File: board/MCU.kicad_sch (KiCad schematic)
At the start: 2 parts, among them IC1 TLT9251VLEXUMA1, IC3 PAC55723QM-T

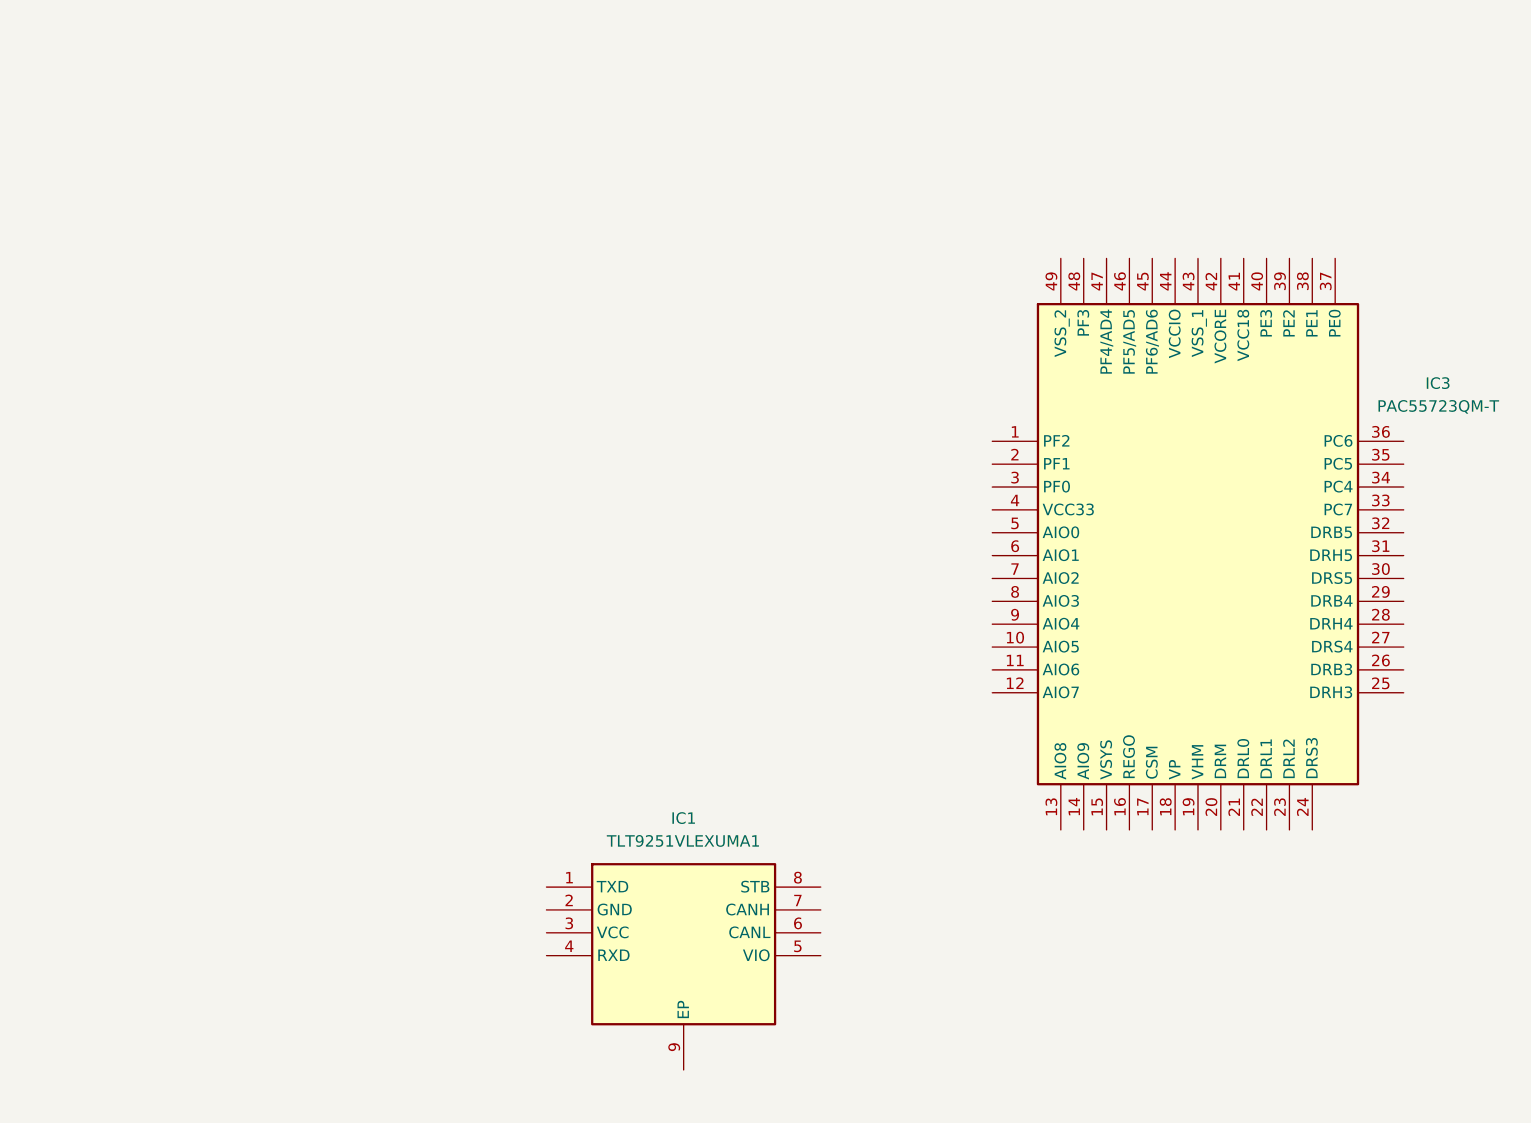
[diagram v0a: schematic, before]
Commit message: Added MCU and initial half bridge circuits from application circuit.
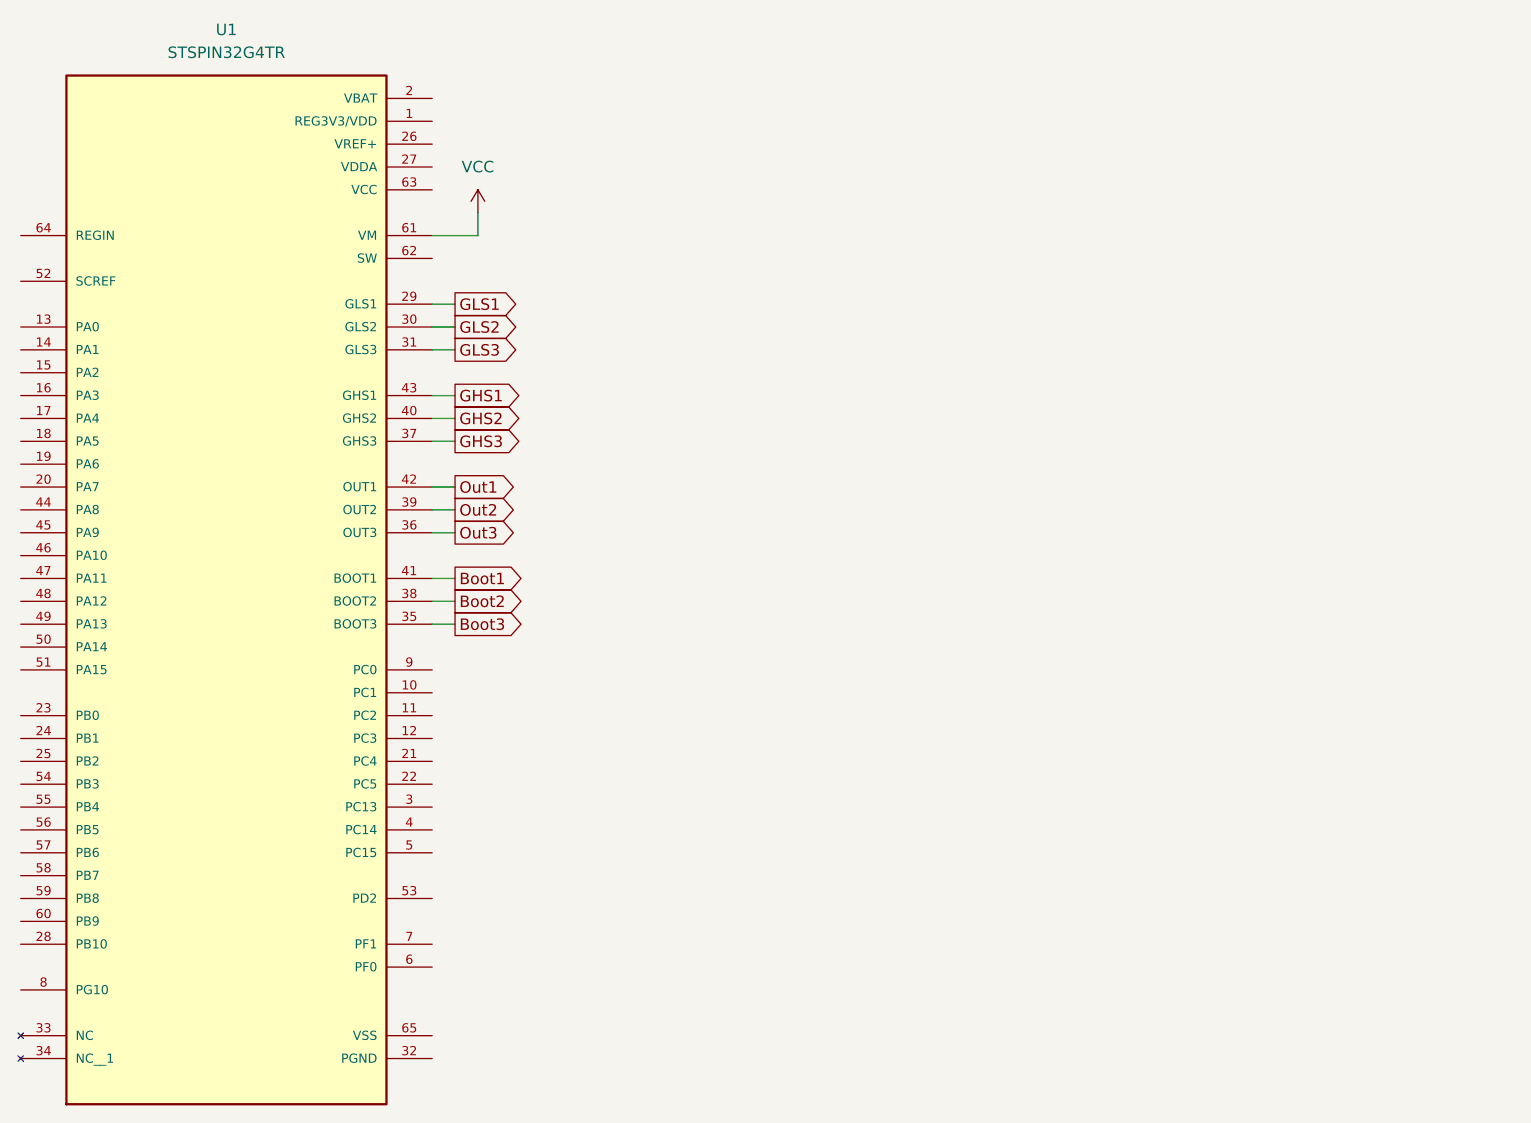
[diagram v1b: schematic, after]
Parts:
- removed IC1: TLT9251VLEXUMA1, brushless_moco_footprints:SON65P300X300X110-9N, symbol brushless_moco_symbols:TLT9251VLEXUMA1
- removed IC3: PAC55723QM-T, brushless_moco_footprints:QFN40P600X600X80-49N-D, symbol brushless_moco_symbols:PAC55723QM-T
- added U1: STSPIN32G4TR, STSPIN32G4TR:QFN50P900X900X100-65N, symbol STSPIN32G4TR:STSPIN32G4TR
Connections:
- new net Boot1: U1.41 (BOOT1)
- new net Boot2: U1.38 (BOOT2)
- new net Boot3: U1.35 (BOOT3)
- new net GHS1: U1.43 (GHS1)
- new net GHS2: U1.40 (GHS2)
- new net GHS3: U1.37 (GHS3)
- new net GLS1: U1.29 (GLS1)
- new net GLS2: U1.30 (GLS2)
- new net GLS3: U1.31 (GLS3)
- new net Out1: U1.42 (OUT1)
- new net Out2: U1.39 (OUT2)
- new net Out3: U1.36 (OUT3)
- new net VCC: U1.61 (VM)

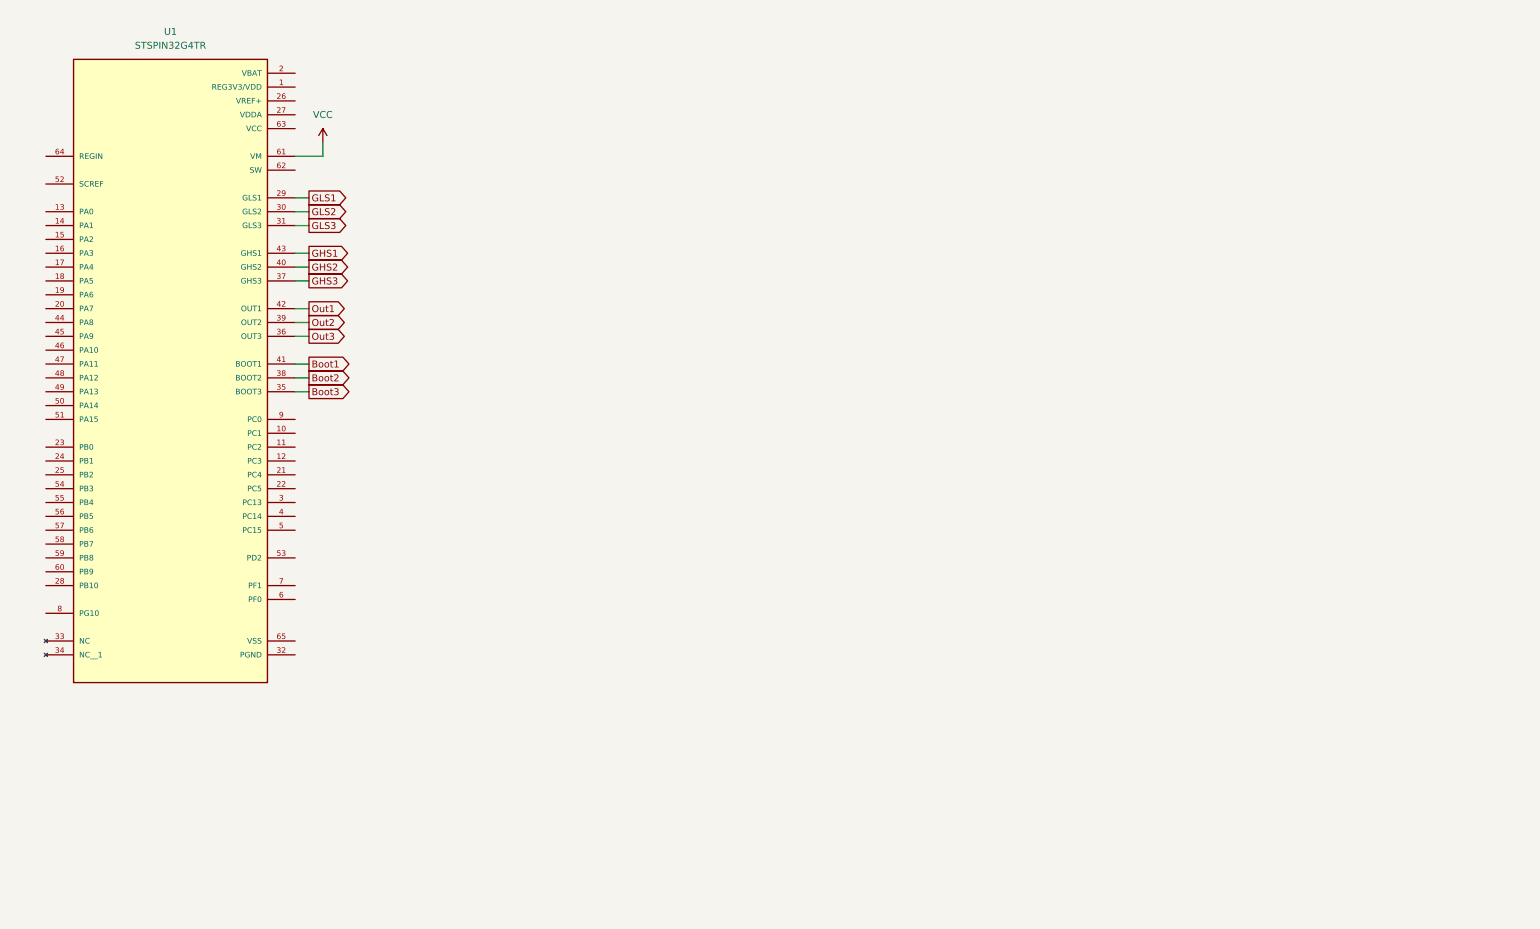
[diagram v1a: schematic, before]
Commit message: Added connections around the MCU from the application circuit from the data sheet, VCC, VDD, VREF+, etc.
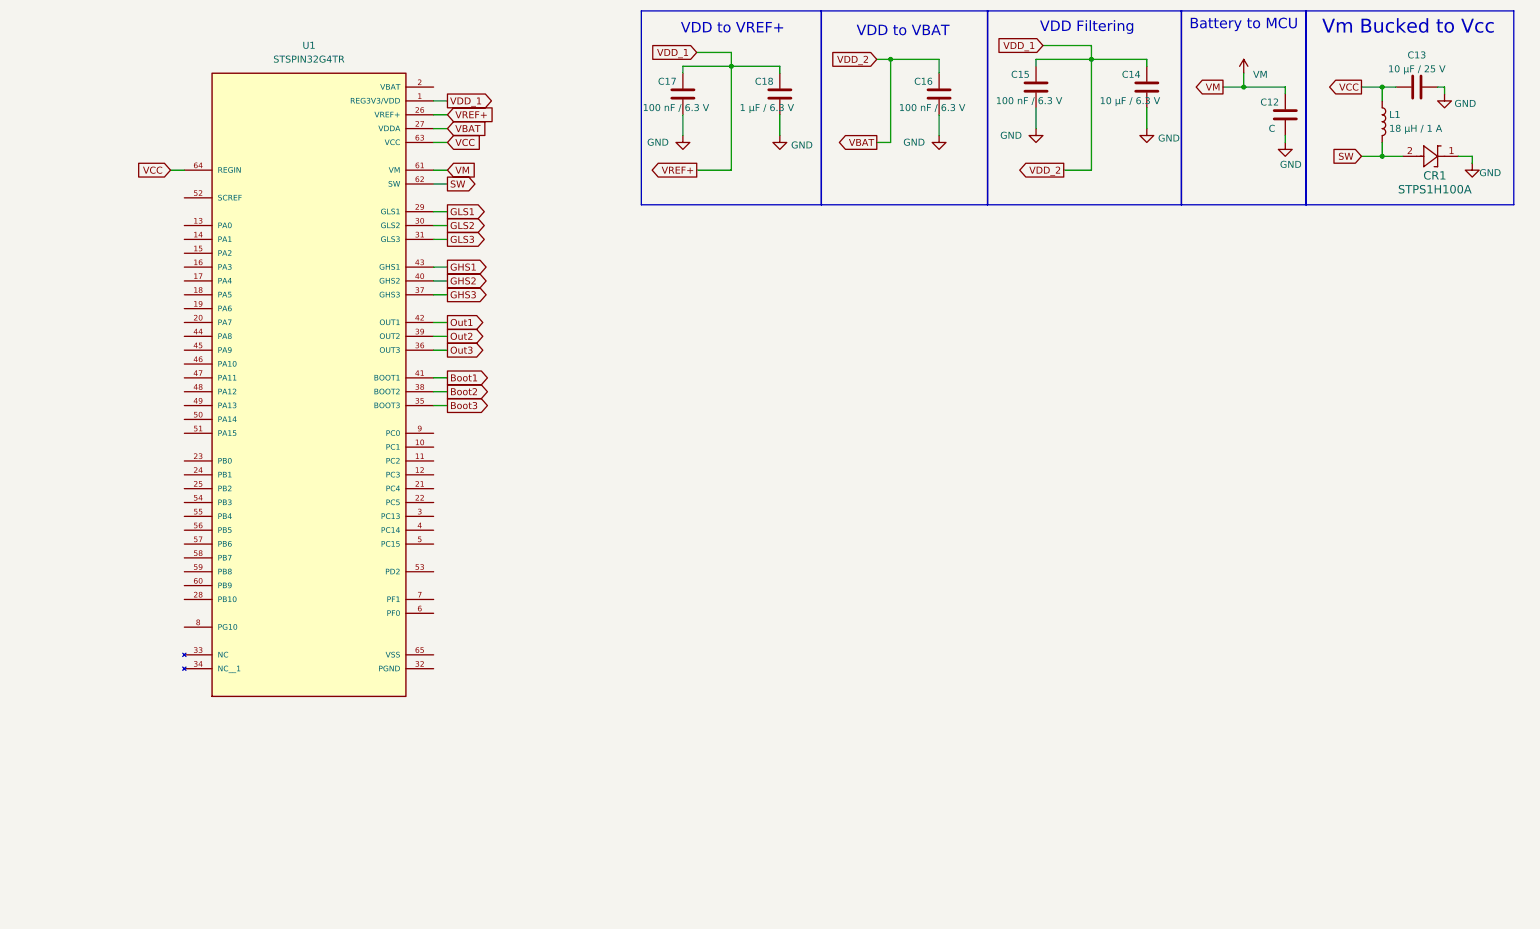
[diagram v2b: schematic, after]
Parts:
- added C12: C, symbol Device:C
- added C13: 10 μF / 25 V, symbol Device:C
- added C14: 10 μF / 6.3 V, symbol Device:C
- added C15, C16, C17: 100 nF / 6.3 V, symbol Device:C
- added C18: 1 μF / 6.3 V, symbol Device:C
- added CR1: STPS1H100A, SMA_STM, symbol STPS1H100A:STPS1H100A
- added L1: 18 μH / 1 A, symbol Device:L
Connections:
- net VCC: now also U1.63 (VCC), U1.64 (REGIN), C13.1, L1.1; no longer U1.61 (VM)
- net VBAT: now reaches U1.1 (REG3V3/VDD)
- net VBAT: now also U1.26 (VREF+), U1.27 (VDDA), C14.1, C15.1, C16.1, C17.1, C18.1
- net SW: now reaches U1.62 (SW)
- net SW: now also CR1.2, L1.2
- new net GND: C12.2, C13.2, C14.2, C15.2, C16.2, C17.2, C18.2, CR1.1
- new net VM: C12.1, U1.61 (VM)
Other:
- note added: "Battery to MCU"
- note added: "VDD Filtering"
- note added: "VDD to VBAT"
- note added: "VDD to VREF+"
- note added: "Vm Bucked to Vcc"
- moved on the sheet: U1

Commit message: Completed basic application circuit from MCU datasheet and adjusted Hierarchical Paths.
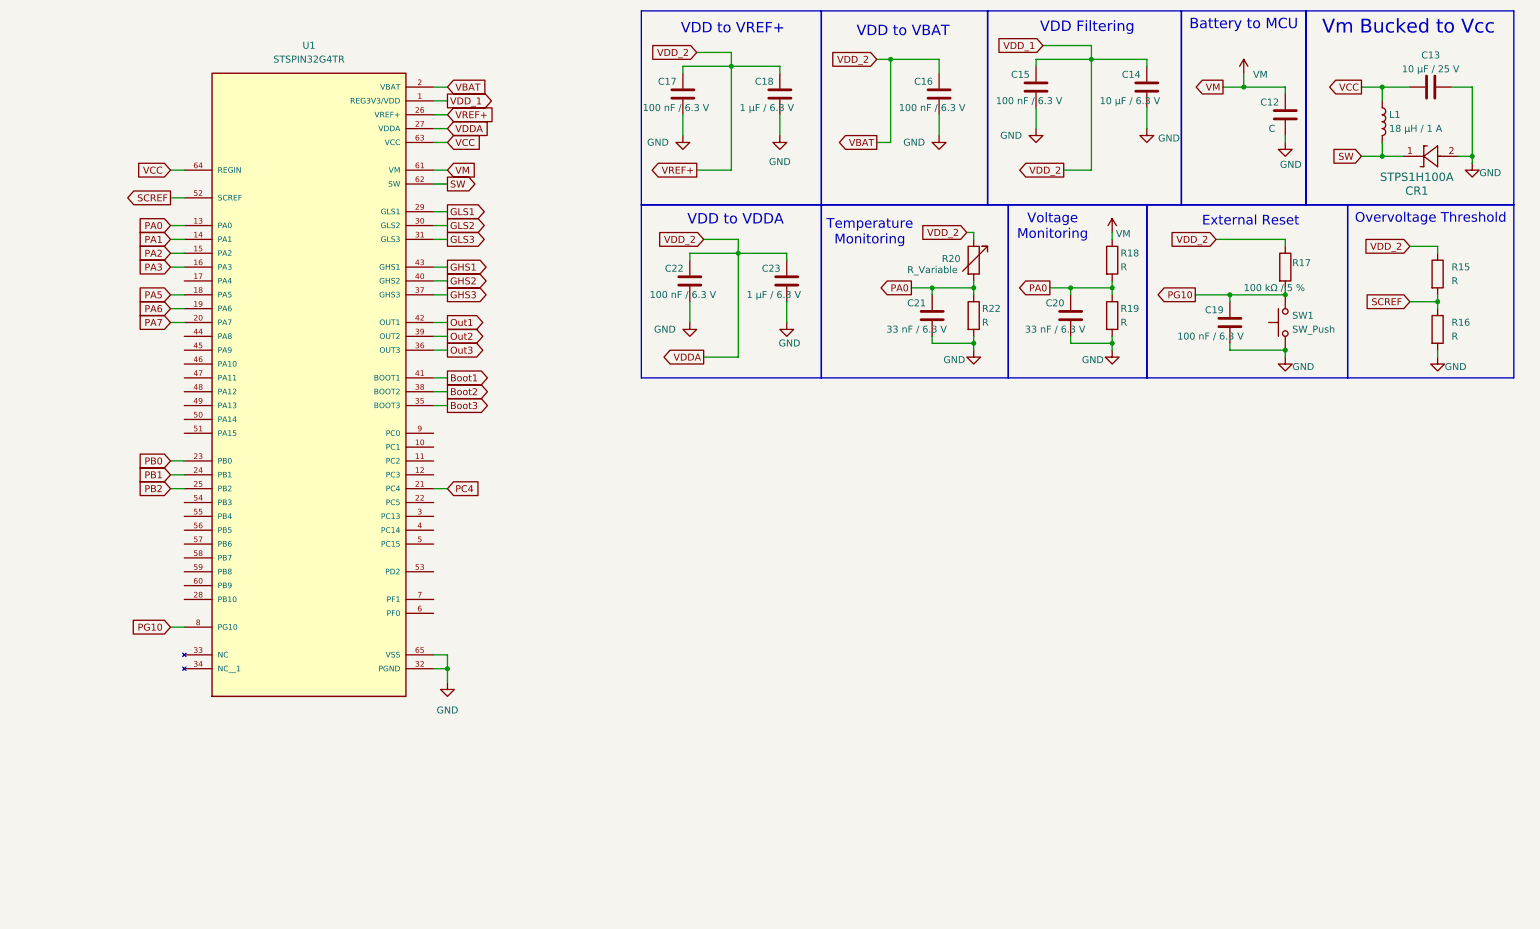
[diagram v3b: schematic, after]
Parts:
- added C19, C22: 100 nF / 6.3 V, symbol Device:C
- added C20, C21: 33 nF / 6.3 V, symbol Device:C
- added C23: 1 μF / 6.3 V, symbol Device:C
- added R15, R16, R18, R19, R22: R, symbol Device:R
- added R17: 100 kΩ / 5 %, symbol Device:R
- added R20: R_Variable, symbol Device:R_Variable
- added SW1: SW_Push, symbol Switch:SW_Push
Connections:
- net GND: now also CR1.2, U1.32 (PGND), U1.65 (VSS), C19.2, C20.2, C21.2, C22.2, C23.2, R16.2, R19.2, R22.2, SW1.1; no longer CR1.1
- net SW: now also CR1.1; no longer CR1.2
- net VBAT: now also U1.2 (VBAT), C22.1, C23.1, R15.1, R17.1, R20.1
- net VM: now also R18.1
- net PA0: now reaches U1.13 (PA0)
- net PA0: now also C20.1, C21.1, R18.2, R19.1, R20.2, R22.1
- net PA1: now reaches U1.14 (PA1)
- net PA2: now reaches U1.15 (PA2)
- net PA3: now reaches U1.16 (PA3)
- net PA5: now reaches U1.18 (PA5)
- net PA6: now reaches U1.19 (PA6)
- net PA7: now reaches U1.20 (PA7)
- net PC4: now reaches U1.21 (PC4)
- net PB0: now reaches U1.23 (PB0)
- net PB1: now reaches U1.24 (PB1)
- net PB2: now reaches U1.25 (PB2)
- net SCREF: now reaches U1.52 (SCREF)
- net SCREF: now also R15.2, R16.1
- net PG10: now reaches U1.8 (PG10)
- net PG10: now also C19.1, R17.2, SW1.2
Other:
- note added: "External Reset"
- note added: "Overvoltage Threshold"
- note added: "Temperature Monitoring"
- note added: "VDD to VDDA"
- note added: "Voltage Monitoring"
- moved on the sheet: C13, CR1
